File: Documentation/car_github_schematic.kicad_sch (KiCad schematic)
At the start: 2 parts, among them J1 Raspberry_Pi_4

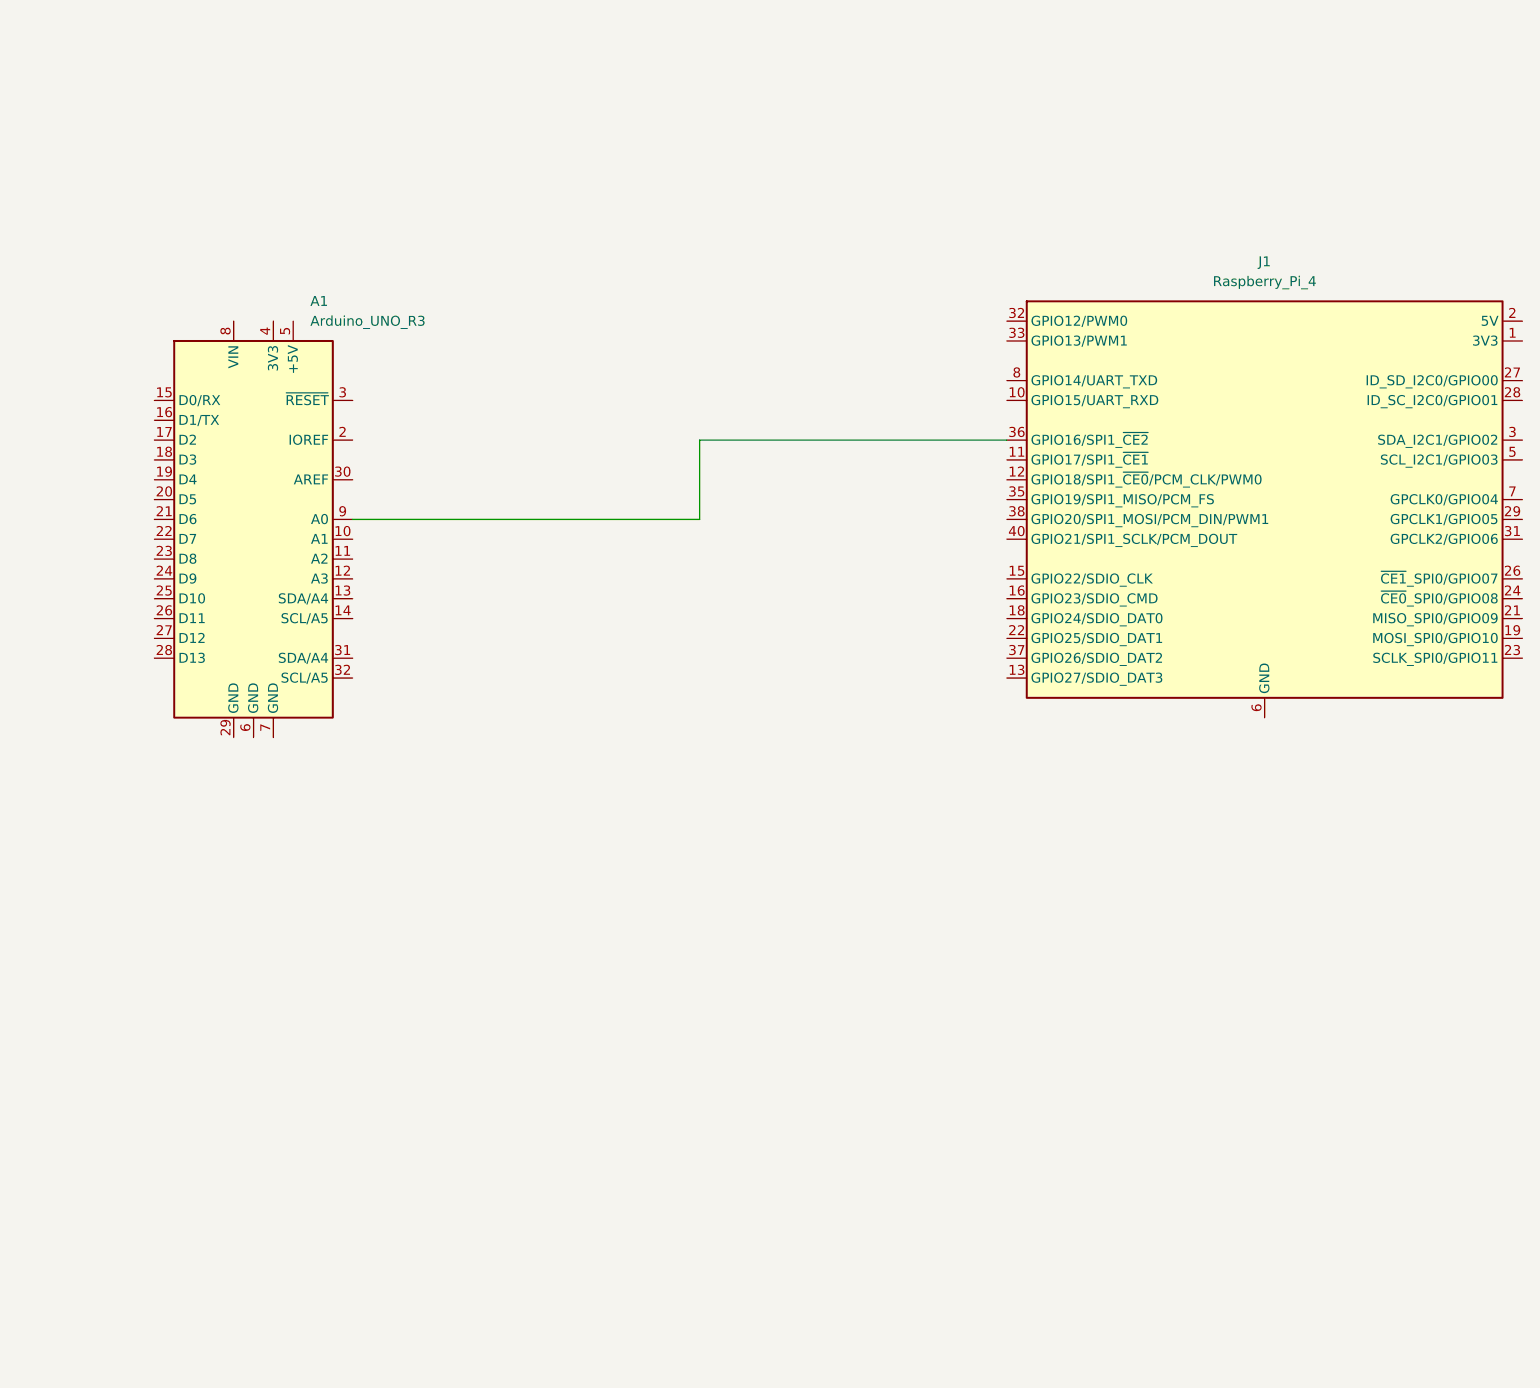
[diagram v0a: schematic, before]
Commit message: added datasheets and implemented a schematic for the vehicle in current state
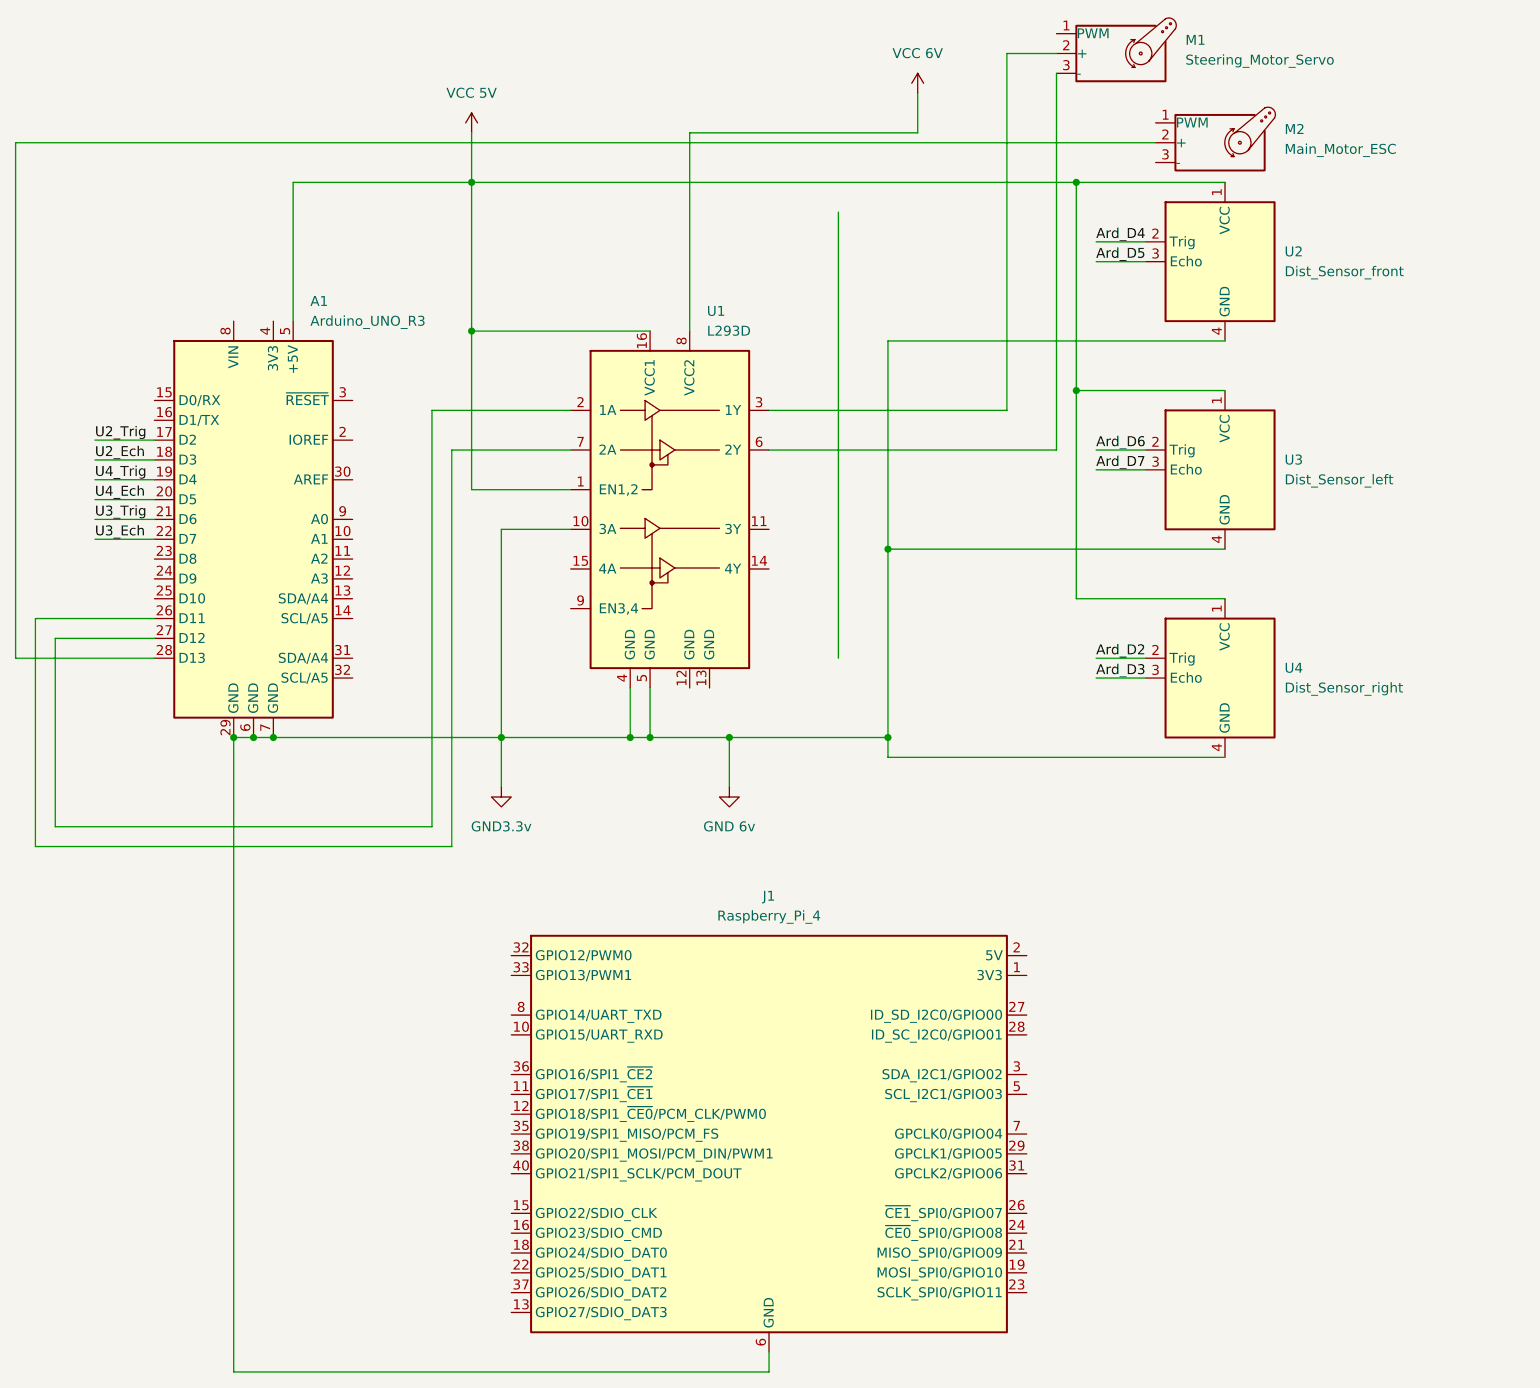
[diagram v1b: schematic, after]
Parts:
- added M1: Steering_Motor_Servo, symbol Motor:Motor_Servo
- added M2: Main_Motor_ESC, symbol Motor:Motor_Servo
- added U1: L293D, Package_DIP:DIP-16_W7.62mm, symbol Driver_Motor:L293D
- added U2: Dist_Sensor_front, Sensor_Distance:HCSR04, symbol Sensor_Distance:TMF8820
- added U3: Dist_Sensor_left, Sensor_Distance:HCSR04, symbol Sensor_Distance:TMF8820
- added U4: Dist_Sensor_right, Sensor_Distance:HCSR04, symbol Sensor_Distance:TMF8820
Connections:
- net U2_Trig: now reaches A1.17 (D2)
- net U2_Ech: now reaches A1.18 (D3)
- net U4_Trig: now reaches A1.19 (D4)
- net U4_Ech: now reaches A1.20 (D5)
- net U3_Trig: now reaches A1.21 (D6)
- net U3_Ech: now reaches A1.22 (D7)
- net at A1.26 (D11): now also U1.7 (2A)
- net at A1.27 (D12): now also U1.2 (1A)
- net at A1.28 (D13): now also M2.2 (+)
- net GND 6v: now reaches A1.29 (GND)
- net GND 6v: now also A1.6 (GND), A1.7 (GND), J1.14 (GND), J1.20 (GND), J1.25 (GND), J1.30 (GND), J1.34 (GND), J1.39 (GND), J1.6 (GND), J1.9 (GND), U1.10 (3A), U1.4 (GND), U1.5 (GND), U2.4 (GND), U3.4 (GND), U4.4 (GND)
- net VCC 5V: now reaches A1.5 (+5V)
- net VCC 5V: now also U1.1 (EN1,2), U1.16 (VCC1), U2.1 (VCC), U2.12 (VDD), U2.7 (VDD), U3.1 (VCC), U3.12 (VDD), U3.7 (VDD), U4.1 (VCC), U4.12 (VDD), U4.7 (VDD)
- net at A1.9 (A0): no longer J1.36 (GPIO16/SPI1_~{CE2})
- new net: U4.4 (GND), U4.8 (GND)
- new net: U3.4 (GND), U3.8 (GND)
- new net: M1.2 (+), U1.3 (1Y)
- new net: M1.3 (-), U1.6 (2Y)
- new net: U2.4 (GND), U2.8 (GND)
- new net Ard_D2: U4.2 (Trig)
- new net Ard_D3: U4.3 (Echo)
- new net Ard_D4: U2.2 (Trig)
- new net Ard_D5: U2.3 (Echo)
- new net Ard_D6: U3.2 (Trig)
- new net Ard_D7: U3.3 (Echo)
- new net VCC 6V: U1.8 (VCC2)
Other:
- moved on the sheet: J1
